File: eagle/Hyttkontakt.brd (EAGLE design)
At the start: 72.4 x 64.4 mm, 12 parts, among them J1 DT15-12PA

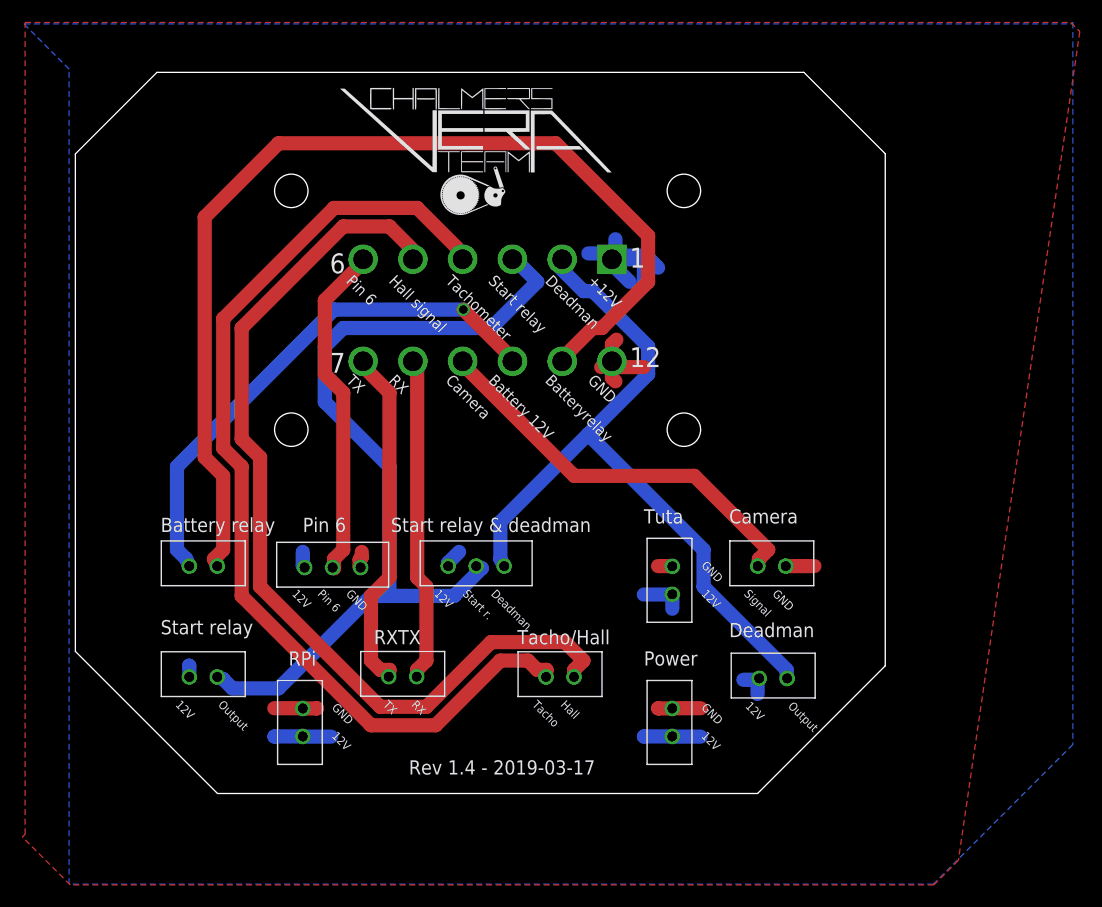
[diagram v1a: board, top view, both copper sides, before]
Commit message: Bypass and easier connections
- HMI now goes on batterybypass connection
- Emergency button has its own connection in serie with HMI and Battery relay button
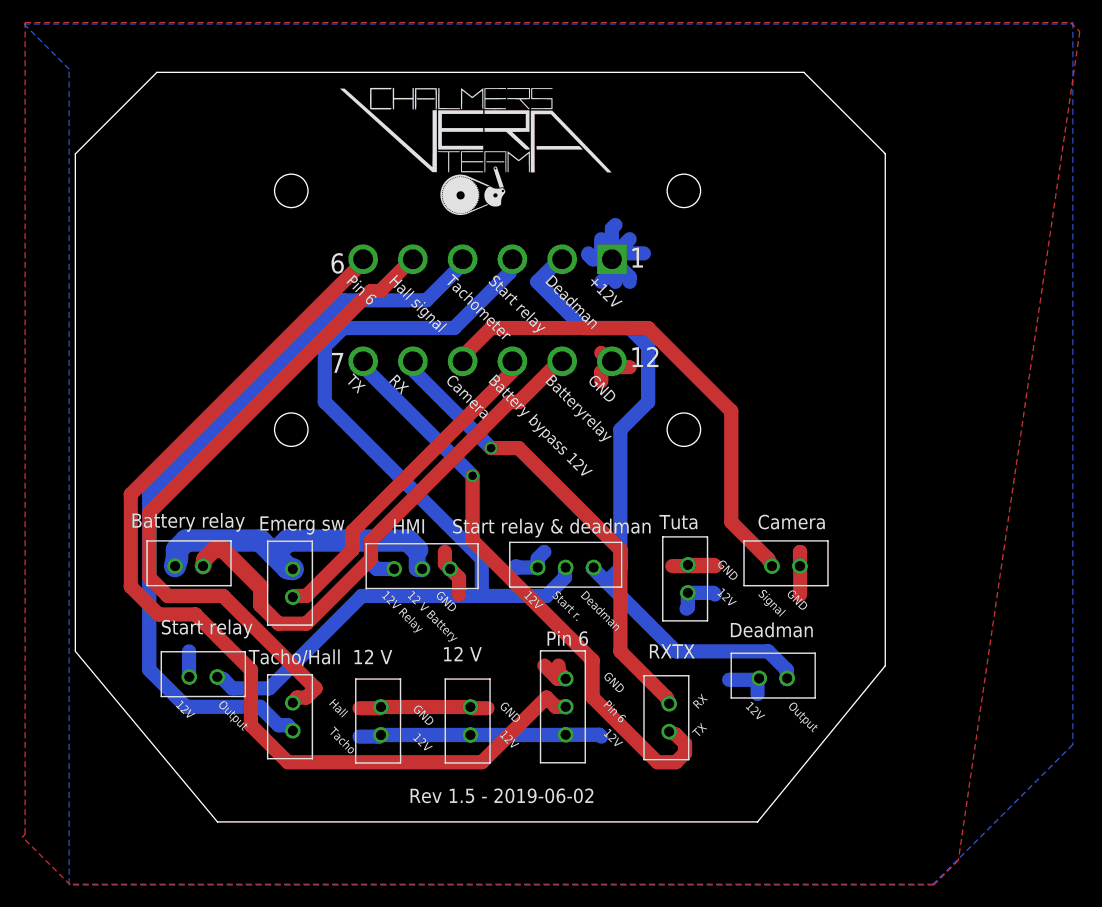
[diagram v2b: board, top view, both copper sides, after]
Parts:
- removed RPI12V: EH_B2B-EH, CASE-JST:B2B-EH
- added EMRGENCYBUTTON, POWER12V1: EH_B2B-EH, CASE-JST:B2B-EH
- added POWERHMI: EH_B3B-EH, CASE-JST:B3B-EH
- moved PIN6 24.3 mm to (43.8, 28.1), turned to 90 degrees
- moved HALL_2PIN 24.1 mm to (19.4, 27.2), turned to 90 degrees
- moved RXTX 24.1 mm to (53.1, 27.1), turned to 90 degrees
- moved POWER12V 18.0 mm to (35.3, 26.8)
- moved STARTANDDEAD 8.00 mm to (43.8, 40.5)
- moved TUTA 1.40 mm to (54.7, 39.5)
- moved KAMERA 1.27 mm to (63.5, 40.6)
- moved BATTERYSTART 1.27 mm to (10.2, 40.6)
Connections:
- net BATTERYSTART renamed BATTERRELAY
- removed net BATTERYSTART12V: BATTERYSTART.1, J1.10
- new net 12VEMERGSWITCH: BATTERYSTART.1, EMRGENCYBUTTON.2, POWERHMI.2
- new net BATTERYBYPASS: EMRGENCYBUTTON.1, J1.10
- net GND: now also POWER12V1.2, POWERHMI.3; no longer RPI12V.2
- net V+: now also POWER12V1.1, POWERHMI.1; no longer RPI12V.1
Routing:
- net PIN6: track 30.2 -> 88.8 mm
- net BATTERYSTART12V: track 47.1 -> 0.00 mm, vias 1 -> 0
- net BATTERRELAY: track 92.9 -> 47.3 mm
- net BATTERYBYPASS: track 0.00 -> 30.4 mm
- net 12VEMERGSWITCH: track 0.00 -> 29.0 mm
- net HALLSIGNAL: track 83.1 -> 60.3 mm
- net TX: track 31.1 -> 52.2 mm, vias 0 -> 1
- net TACHOMETER: track 88.6 -> 67.8 mm
- net V+: track 38.1 -> 58.3 mm
- net GND: track 21.3 -> 35.8 mm
- net RX: track 29.0 -> 41.9 mm, vias 0 -> 1
- net KAMERASIGNAL: track 36.2 -> 43.8 mm
- net STARTMOTOR: track 78.1 -> 85.1 mm
- net DEADMAN: track 66.5 -> 60.0 mm
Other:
- board size 72.4 x 64.4 mm -> 72.4 x 67 mm
- board text added: "12 V"
- board text added: "12 V Battery"
- board text added: "12V Relay"
- board text added: "Battery bypass 12V"
- board text added: "Emerg sw"
- board text added: "HMI"
- board text added: "Rev 1.5 - 2019-06-02"
- board text removed: "Battery 12V"
- board text removed: "Power"
- board text removed: "RPi"
- board text removed: "Rev 1.4 - 2019-03-17"
